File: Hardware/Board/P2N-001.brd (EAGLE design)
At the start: 72 x 72 mm, 37 parts, among them IC1 4053N, IC2 LTC485N, IC3 74LS07N, IC4 LTC485N, K1 G5V1, T1 2SC1815, X1 HIROSE-DX10LM1-14SE

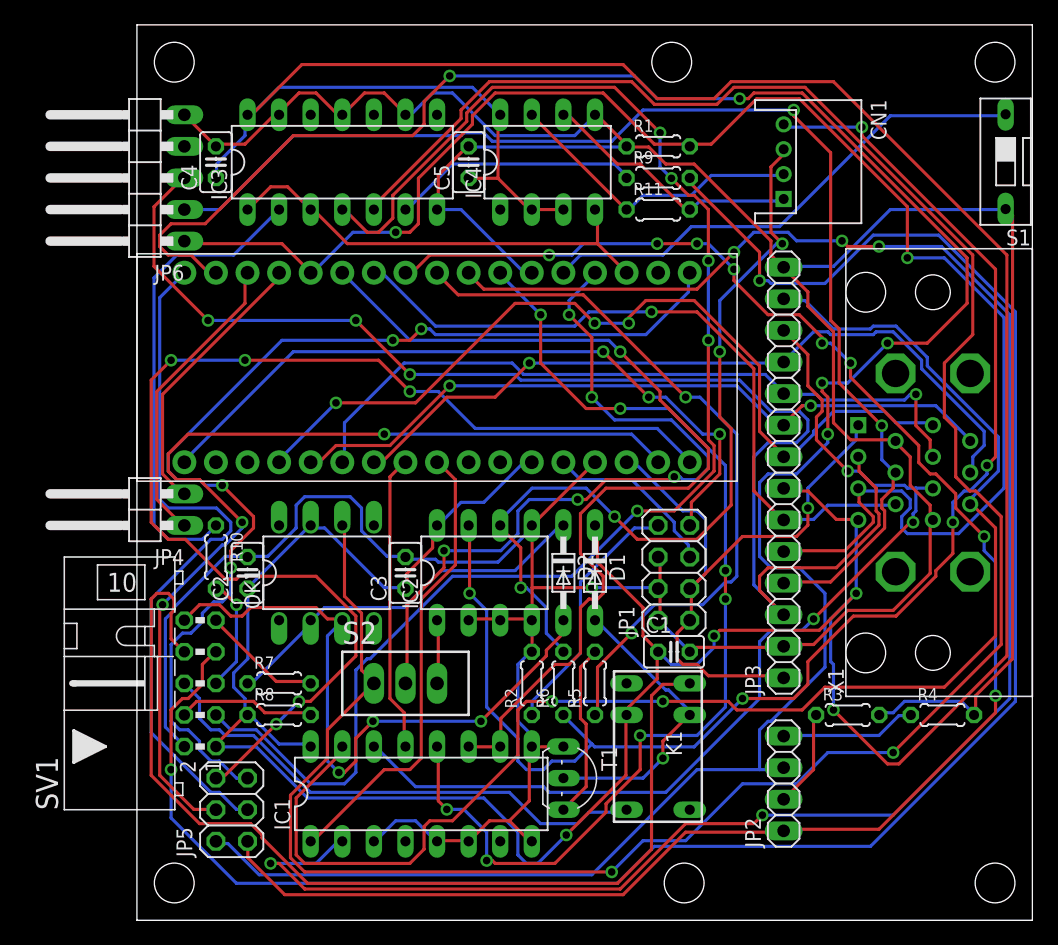
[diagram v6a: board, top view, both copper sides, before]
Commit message: Changed 10p-backport to 14p-backport.
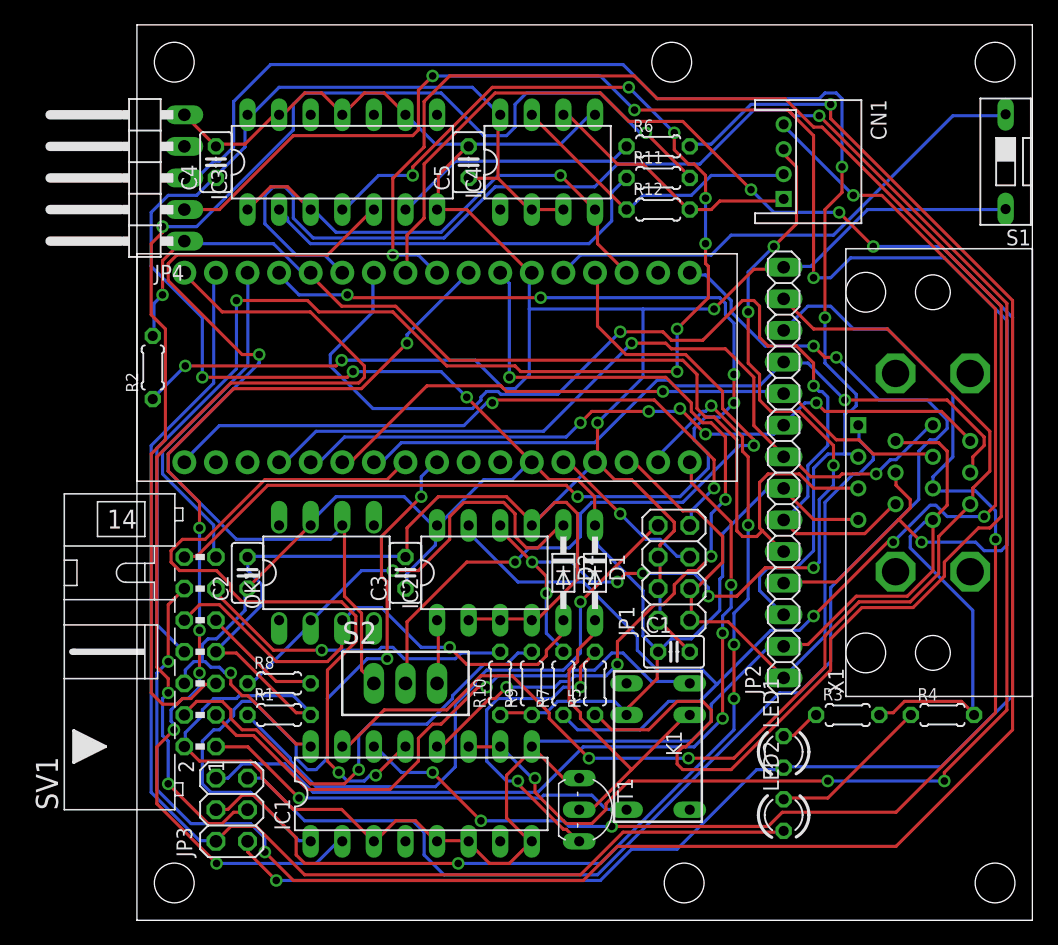
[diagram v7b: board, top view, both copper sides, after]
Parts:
- removed JP5: (no value), pinhead:2X03
- removed JP6: (no value), pinhead:1X05/90
- added LED1, LED2: (no value), led:LED3MM
- added R12: 120, resistor:0204/5
- JP2: device pinhead:1X04 -> pinhead:1X14
- JP3: device pinhead:1X14 -> pinhead:2X03
- JP4: device pinhead:1X02/90 -> pinhead:1X05/90
- R1: value 10k -> 150
- R11, R6: value 120 -> 220
- R2: value 150 -> 10k
- R7: value 220 -> 120
- SV1: device con-ml:ML10L -> con-ml:ML14L
- moved R1 54.9 mm to (11.4, 16.5)
- moved JP3 52.0 mm to (7.62, 8.89)
- moved R6 43.8 mm to (41.9, 62.2), turned to 0 degrees
- moved R9 41.9 mm to (31.8, 19.1), turned to 90 degrees
- moved R2 39.7 mm to (1.27, 44.5)
- moved JP4 26.7 mm to (0.00, 59.7)
- moved R10 25.0 mm to (29.2, 19.1), turned to 90 degrees
- moved JP2 25.0 mm to (52.0, 36.0)
- moved R7 22.9 mm to (34.3, 19.1), turned to 90 degrees
- moved T1 2.84 mm to (35.6, 8.89)
- moved R11 2.54 mm to (41.9, 59.7)
- moved R8 2.54 mm to (11.4, 19.1)
- moved SV1 2.54 mm to (5.08, 21.6)
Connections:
- removed net SX: JP4.1, MC1.P$3
- removed net SY: JP4.2, MC1.P$4
- new net N$5: R10.2, SV1.11
- new net SENS0: MC1.P$3, SV1.13
- new net SENS1: MC1.P$4, SV1.14
- net ANLG0: now also JP2.8; no longer JP3.8
- net ANLG1: now also JP2.9; no longer JP3.9
- net ANLG2: now also JP2.10; no longer JP3.10
- net ANLG3: now also JP2.11; no longer JP3.11
- net CA: now also SV1.1; no longer SV1.6
- net CB: now also SV1.3; no longer SV1.8
- net CD: now also JP2.6; no longer JP3.6
- net GND: now also JP2.14, JP2.2, JP4.5, R1.2, R2.1, SV1.7; no longer JP3.14, JP3.2, JP6.5, R1.1, R2.2
- net GPIO0: now also JP3.1, LED1.A; no longer JP2.1, JP5.1
- net GPIO1: now also JP3.2, LED2.A; no longer JP2.3, JP5.2
- net GPIO2: now also JP3.3; no longer JP5.3
- net MISO: now also JP3.4; no longer JP5.4
- net MOSI: now also JP3.5; no longer JP5.5
- net N$15: now also R8.1; no longer R7.1
- net N$17: now also LED1.K; no longer JP2.2
- net N$18: now also LED2.K; no longer JP2.4
- net N$2: now also R11.1; no longer R10.1
- net N$28: now also JP2.12; no longer JP3.12
- net N$29: now also JP2.13; no longer JP3.13
- net N$3: now also R6.1; no longer R9.1
- net N$32: now also R1.1; no longer R2.1
- net N$4: now also R6.2, SV1.12; no longer R9.2, SV1.7
- net PD: now also JP2.5, JP4.1, R2.2; no longer JP3.5, JP6.1, R1.2
- net RAWTX: now also SV1.8; no longer SV1.3
- net RETURN: now also R11.2; no longer R10.2
- net RX+: now also R7.2; no longer R6.2
- net RX-: now also R7.1; no longer R6.1
- net RXA: now also R8.2; no longer R7.2
- net SCLK: now also JP3.6; no longer JP5.6
- net SEND: now also R9.2; no longer R8.2
- net TX+: now also R12.2; no longer R11.2
- net TX-: now also R12.1; no longer R11.1
- net USBD+: now also JP2.3, JP4.3; no longer JP3.3, JP6.3
- net USBD-: now also JP2.4, JP4.2; no longer JP3.4, JP6.2
- net VCC: now also JP2.7, R10.1, R9.1, SV1.6; no longer JP3.7, R8.1, SV1.1
- net VDD: now also JP2.1; no longer JP3.1
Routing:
- net MIDIRX: track 190.2 -> 72.4 mm, vias 2 -> 1
- net VCC: track 324.8 -> 215.8 mm
- net SENS1: track 0.00 -> 98.9 mm, vias 0 -> 5
- net GPIO1: track 193.1 -> 100.0 mm, vias 5 -> 0
- net SEL: track 75.6 -> 167.2 mm, vias 1 -> 4
- net RETURN: track 9.23 -> 99.9 mm, vias 1 -> 2
- net RELAY: track 59.4 -> 142.9 mm, vias 2 -> 1
- net SCL: track 152.8 -> 79.3 mm, vias 5 -> 6
- net GND: track 340.5 -> 391.3 mm, vias 1 -> 4
- net PD: track 130.9 -> 86.5 mm, vias 2 -> 1
- net ANLG4: track 23.9 -> 60.3 mm, vias 0 -> 2
- net CB: track 82.1 -> 47.2 mm, vias 0 -> 1
- net USBD-: track 100.4 -> 132.6 mm, vias 2 -> 4
- net SCLK: track 97.1 -> 66.9 mm, vias 5 -> 3
- net N$32: track 20.5 -> 49.8 mm, vias 0 -> 1
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
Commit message: Adopted to XMIDI.
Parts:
- added R13: 220, resistor:0204/5
- added R14: 120, resistor:0204/5
- R12: value 120 -> 220
- moved R11 41.0 mm to (36.8, 19.1), turned to 90 degrees
- moved R5 13.0 mm to (39.4, 6.35), turned to 0 degrees
- moved R10 5.08 mm to (34.3, 19.1)
- moved R12 5.08 mm to (41.9, 62.2)
- moved R7 5.08 mm to (29.2, 19.1)
- moved R6 2.54 mm to (41.9, 64.8)
- moved T1 2.54 mm to (35.6, 11.4)
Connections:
- removed net CA: K1.5, SV1.1
- removed net CB: K1.10, SV1.3
- removed net N$5: R10.2, SV1.11
- removed net RAWTX: IC3.4, SV1.8
- removed net RETURN: R11.2, SV1.5
- removed net SEND: R9.2, SV1.4
- new net RXRETURN: R6.2, SV1.3
- new net RXSEND: R11.2, SV1.1
- new net TXRETURN: R13.2, SV1.8
- new net TXRETURNII: R12.2, SV1.5
- new net TXSEND: R9.2, SV1.6
- new net TXSENDZV: R10.2, SV1.14, SV1.4
- new net ZVA: K1.5, SV1.11
- new net ZVB: K1.10, SV1.13
- net GND: now also SV1.12
- net N$2: now also R12.1; no longer R11.1
- net N$4: now also IC3.4, R13.1; no longer R6.2, SV1.12
- net SENS0: no longer SV1.13
- net SENS1: no longer SV1.14
- net TX+: now also R14.2; no longer R12.2
- net TX-: now also R14.1; no longer R12.1
- net VCC: now also R11.1; no longer SV1.6
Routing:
- net TXRETURNII: track 0.00 -> 148.6 mm, vias 0 -> 2
- net N$4: track 163.7 -> 30.9 mm, vias 3 -> 0
- net RAWTX: track 124.0 -> 0.00 mm, vias 8 -> 0
- net RXRETURN: track 0.00 -> 103.5 mm, vias 0 -> 2
- net RETURN: track 99.9 -> 0.00 mm, vias 2 -> 0
- net SENS1: track 98.9 -> 0.00 mm, vias 5 -> 0
- net SEL: track 167.2 -> 79.9 mm
- net TXRETURN: track 0.00 -> 86.8 mm, vias 0 -> 2
- net SCL: track 79.3 -> 154.6 mm, vias 6 -> 4
- net SDA: track 68.4 -> 142.6 mm, vias 5 -> 4
- net TXSENDZV: track 0.00 -> 67.3 mm, vias 0 -> 3
- net ZVB: track 0.00 -> 67.0 mm, vias 0 -> 1
- net GPIO0: track 166.4 -> 110.2 mm, vias 4 -> 3
- net RXSEND: track 0.00 -> 54.1 mm, vias 0 -> 3
- net ZVA: track 0.00 -> 53.7 mm, vias 0 -> 1
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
